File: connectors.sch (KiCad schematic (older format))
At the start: 43 parts, among them J10 70543-0001, J11 70543-0001, J12 70543-0001, J13 70543-0001, J14 70543-0003, J15 Conn_02x20_Odd_Even, J22 70543-0002, J23 70543-0002, J24 70543-0002, J5 20021121-00010C4LF, J6 70543-0001, J7 70543-0001, J8 70543-0001, J9 70543-0001

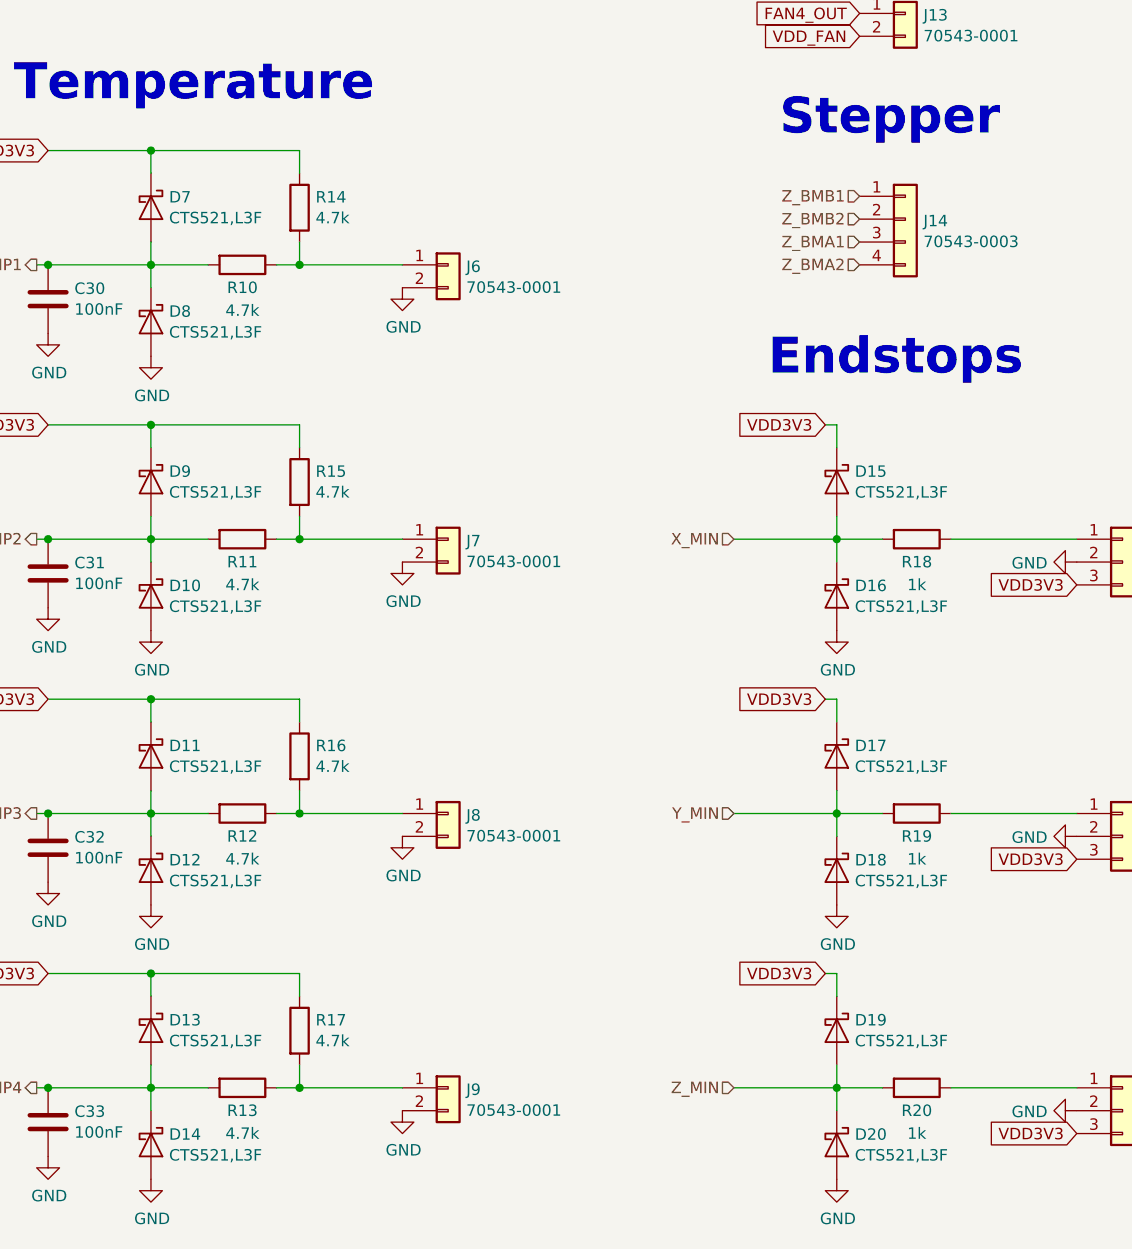
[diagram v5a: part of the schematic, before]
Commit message: Various changes
* Add Status LED
* Switched small diodes to more general available BAT54 in SOD123
* Fixed various DRC errors
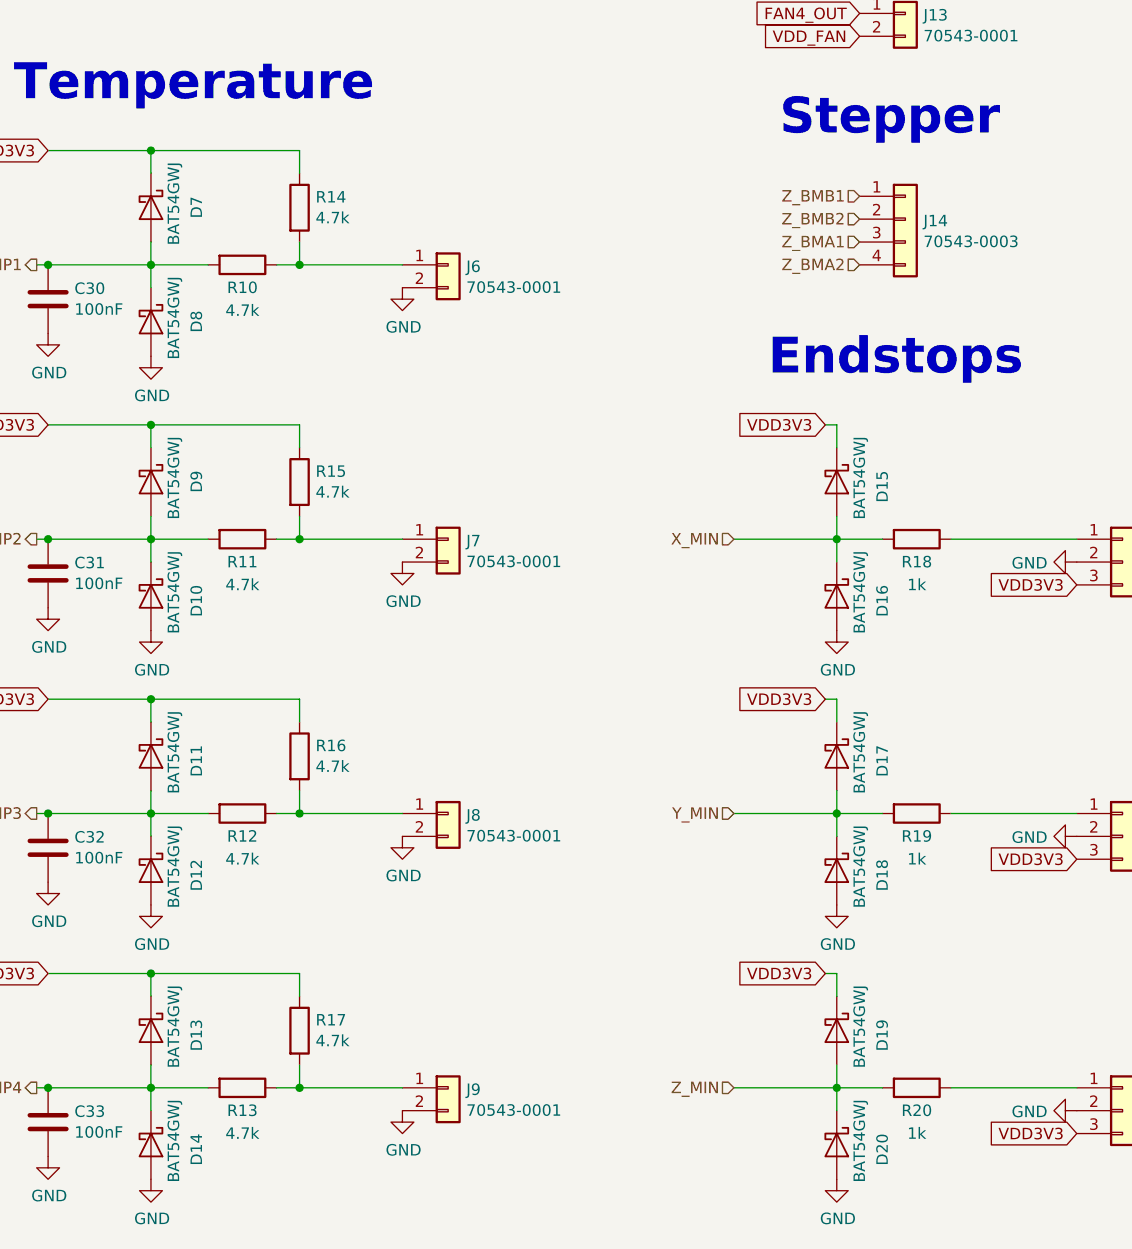
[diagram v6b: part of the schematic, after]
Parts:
- D10, D11, D12, D13, D14, D15, D16, D17, D18, D19, D20, D7, D8, D9: value CTS521,L3F -> BAT54GWJ; footprint heteromycin:SOD882 -> Diode_SMD:D_SOD-123

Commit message: Complete functional design
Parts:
- renumbered C30 to C110, C31 to C111, C32 to C112, C33 to C113, D7 to D19, D8 to D20, D9 to D21, D10 to D22, D11 to D23, D12 to D24, D13 to D25, D14 to D26, D15 to D27, D16 to D28, D17 to D29, D18 to D30, D19 to D31, D20 to D32, J5 to J11, J6 to J12, J7 to J13, J8 to J14, J9 to J15, J10 to J16, J11 to J17, J12 to J18, J13 to J19, J14 to J20, J22 to J21, J23 to J22, J24 to J23, J15 to J24, R10 to R117, R11 to R118, R12 to R119, R13 to R120, R14 to R121, R15 to R122, R16 to R123, R17 to R124, R18 to R125, R19 to R126, R20 to R127

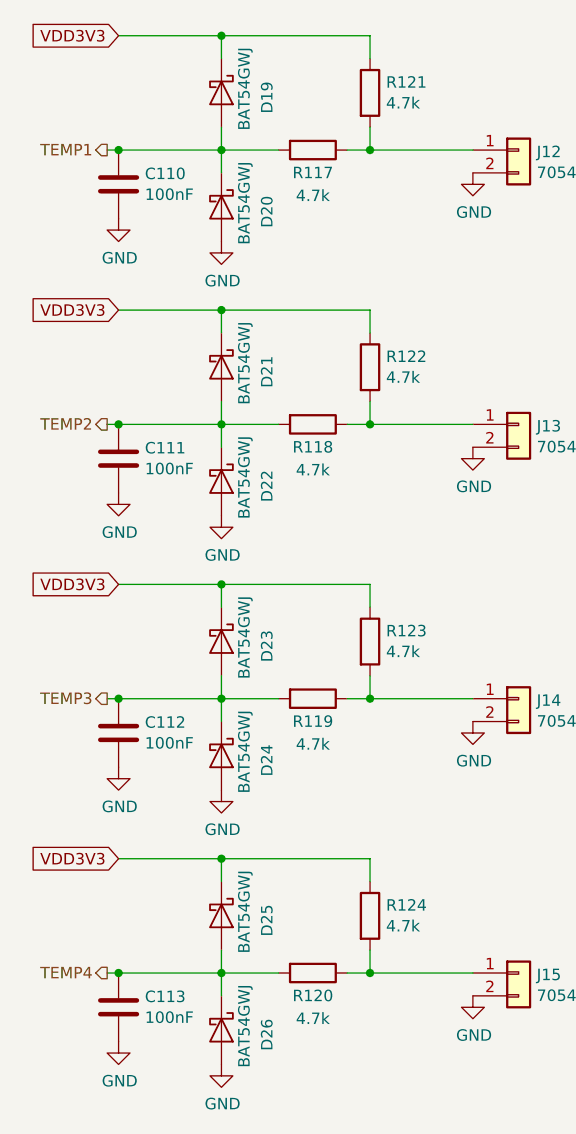
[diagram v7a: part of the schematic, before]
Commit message: Add bypass cap for I2C EEPROMs and redone some copper pour
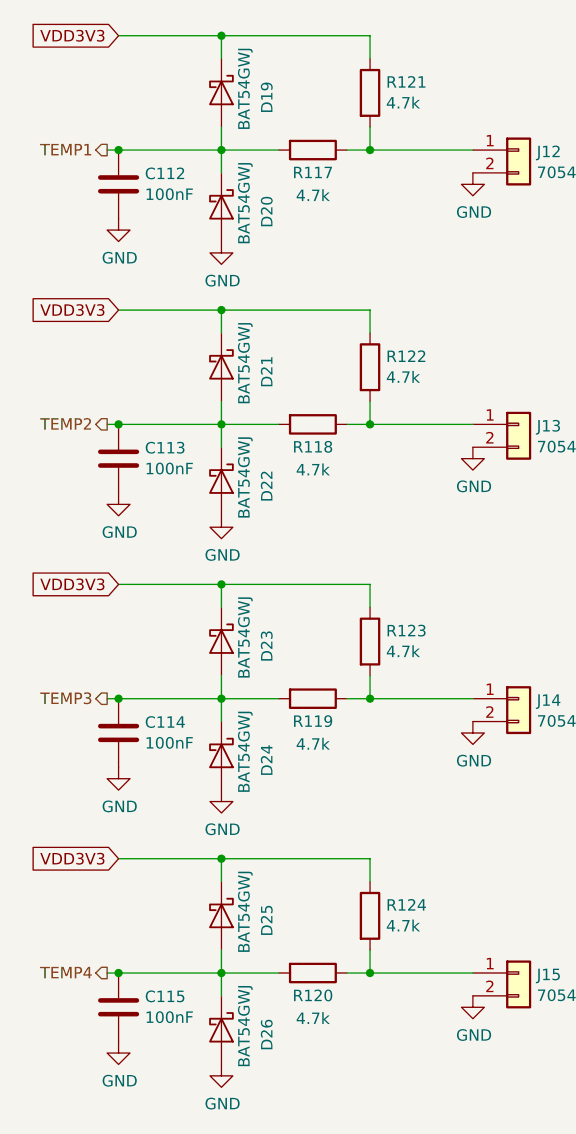
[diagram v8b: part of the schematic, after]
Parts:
- renumbered C110 to C112, C111 to C113, C112 to C114, C113 to C115
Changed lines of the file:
@@
 $EndComp
 $Comp
-L power:GND #PWR0116
+L power:GND #PWR0118
 U 1 1 5B1719B0
 P 1500 3700
-F 0 "#PWR0116" H 1500 3450 50  0001 C CNN
+F 0 "#PWR0118" H 1500 3450 50  0001 C CNN
 F 1 "GND" H 1505 3527 50  0000 C CNN
 F 2 "" H 1500 3700 50  0001 C CNN
@@
 $EndComp
 $Comp
-L power:GND #PWR0120
+L power:GND #PWR0122
 U 1 1 5B1719CA
 P 2600 3400
-F 0 "#PWR0120" H 2600 3150 50  0001 C CNN
+F 0 "#PWR0122" H 2600 3150 50  0001 C CNN
 F 1 "GND" H 2605 3227 50  0000 C CNN
 F 2 "" H 2600 3400 50  0001 C CNN
@@
 $EndComp
 $Comp
-L Device:C C110
+L Device:C C112
 U 1 1 5B1719D4
 P 1050 3450
-F 0 "C110" H 1165 3496 50  0000 L CNN
+F 0 "C112" H 1165 3496 50  0000 L CNN
 F 1 "100nF" H 1165 3405 50  0000 L CNN
 F 2 "Capacitor_SMD:C_0603_1608Metric" H 1088 3300 50  0001 C CNN
@@
 	1000 3300 1050 3300
 $Comp
-L power:GND #PWR0111
+L power:GND #PWR0113
 U 1 1 5B1719DF
 P 1050 3600
-F 0 "#PWR0111" H 1050 3350 50  0001 C CNN
+F 0 "#PWR0113" H 1050 3350 50  0001 C CNN
 F 1 "GND" H 1055 3427 50  0000 C CNN
 F 2 "" H 1050 3600 50  0001 C CNN
@@
 TEMP2
 $Comp
-L power:GND #PWR0121
+L power:GND #PWR0123
 U 1 1 5B171A2B
 P 2600 4600
-F 0 "#PWR0121" H 2600 4350 50  0001 C CNN
+F 0 "#PWR0123" H 2600 4350 50  0001 C CNN
 F 1 "GND" H 2605 4427 50  0000 C CNN
 F 2 "" H 2600 4600 50  0001 C CNN
@@
 TEMP3
 $Comp
-L power:GND #PWR0122
+L power:GND #PWR0124
 U 1 1 5B171A8C
 P 2600 5800
-F 0 "#PWR0122" H 2600 5550 50  0001 C CNN
+F 0 "#PWR0124" H 2600 5550 50  0001 C CNN
 F 1 "GND" H 2605 5627 50  0000 C CNN
 F 2 "" H 2600 5800 50  0001 C CNN
@@
 $EndComp
 $Comp
-L power:GND #PWR0115
+L power:GND #PWR0117
 U 1 1 5B17C4C4
 P 1150 1850
-F 0 "#PWR0115" H 1150 1600 50  0001 C CNN
+F 0 "#PWR0117" H 1150 1600 50  0001 C CNN
 F 1 "GND" H 1155 1677 50  0000 C CNN
 F 2 "" H 1150 1850 50  0001 C CNN
@@
 $EndComp
 $Comp
-L power:GND #PWR0124
+L power:GND #PWR0126
 U 1 1 5B40FD91
 P 4500 4900
-F 0 "#PWR0124" H 4500 4650 50  0001 C CNN
+F 0 "#PWR0126" H 4500 4650 50  0001 C CNN
 F 1 "GND" H 4505 4727 50  0000 C CNN
 F 2 "" H 4500 4900 50  0001 C CNN
@@
 $EndComp
 $Comp
-L power:GND #PWR0125
+L power:GND #PWR0127
 U 1 1 5B453620
 P 4500 6100
-F 0 "#PWR0125" H 4500 5850 50  0001 C CNN
+F 0 "#PWR0127" H 4500 5850 50  0001 C CNN
 F 1 "GND" H 4505 5927 50  0000 C CNN
 F 2 "" H 4500 6100 50  0001 C CNN
@@
 $EndComp
 $Comp
-L power:GND #PWR0126
+L power:GND #PWR0128
 U 1 1 5B457725
 P 4500 7300
-F 0 "#PWR0126" H 4500 7050 50  0001 C CNN
+F 0 "#PWR0128" H 4500 7050 50  0001 C CNN
 F 1 "GND" H 4505 7127 50  0000 C CNN
 F 2 "" H 4500 7300 50  0001 C CNN
@@
 $EndComp
 $Comp
-L power:GND #PWR0117
+L power:GND #PWR0119
 U 1 1 5B565802
 P 1500 4900
-F 0 "#PWR0117" H 1500 4650 50  0001 C CNN
+F 0 "#PWR0119" H 1500 4650 50  0001 C CNN
 F 1 "GND" H 1505 4727 50  0000 C CNN
 F 2 "" H 1500 4900 50  0001 C CNN
@@
 	2150 4500 2150 4400
 $Comp
-L Device:C C111
+L Device:C C113
 U 1 1 5B56580A
 P 1050 4650
-F 0 "C111" H 1165 4696 50  0000 L CNN
+F 0 "C113" H 1165 4696 50  0000 L CNN
 F 1 "100nF" H 1165 4605 50  0000 L CNN
 F 2 "Capacitor_SMD:C_0603_1608Metric" H 1088 4500 50  0001 C CNN
@@
 	1000 4500 1050 4500
 $Comp
-L power:GND #PWR0112
+L power:GND #PWR0114
 U 1 1 5B565812
 P 1050 4800
-F 0 "#PWR0112" H 1050 4550 50  0001 C CNN
+F 0 "#PWR0114" H 1050 4550 50  0001 C CNN
 F 1 "GND" H 1055 4627 50  0000 C CNN
 F 2 "" H 1050 4800 50  0001 C CNN
@@
 $EndComp
 $Comp
-L power:GND #PWR0118
+L power:GND #PWR0120
 U 1 1 5B57C5C8
 P 1500 6100
-F 0 "#PWR0118" H 1500 5850 50  0001 C CNN
+F 0 "#PWR0120" H 1500 5850 50  0001 C CNN
 F 1 "GND" H 1505 5927 50  0000 C CNN
 F 2 "" H 1500 6100 50  0001 C CNN
@@
 	2150 5700 2150 5600
 $Comp
-L Device:C C112
+L Device:C C114
 U 1 1 5B57C5D0
 P 1050 5850
-F 0 "C112" H 1165 5896 50  0000 L CNN
+F 0 "C114" H 1165 5896 50  0000 L CNN
 F 1 "100nF" H 1165 5805 50  0000 L CNN
 F 2 "Capacitor_SMD:C_0603_1608Metric" H 1088 5700 50  0001 C CNN
@@
 	1000 5700 1050 5700
 $Comp
-L power:GND #PWR0113
+L power:GND #PWR0115
 U 1 1 5B57C5D8
 P 1050 6000
-F 0 "#PWR0113" H 1050 5750 50  0001 C CNN
+F 0 "#PWR0115" H 1050 5750 50  0001 C CNN
 F 1 "GND" H 1055 5827 50  0000 C CNN
 F 2 "" H 1050 6000 50  0001 C CNN
@@
 TEMP4
 $Comp
-L power:GND #PWR0123
+L power:GND #PWR0125
 U 1 1 5BC9839A
 P 2600 7000
-F 0 "#PWR0123" H 2600 6750 50  0001 C CNN
+F 0 "#PWR0125" H 2600 6750 50  0001 C CNN
 F 1 "GND" H 2605 6827 50  0000 C CNN
 F 2 "" H 2600 7000 50  0001 C CNN
@@
 $EndComp
 $Comp
-L power:GND #PWR0119
+L power:GND #PWR0121
 U 1 1 5BC983B5
 P 1500 7300
-F 0 "#PWR0119" H 1500 7050 50  0001 C CNN
+F 0 "#PWR0121" H 1500 7050 50  0001 C CNN
 F 1 "GND" H 1505 7127 50  0000 C CNN
 F 2 "" H 1500 7300 50  0001 C CNN
@@
 	2150 6900 2150 6800
 $Comp
-L Device:C C113
+L Device:C C115
 U 1 1 5BC983BD
 P 1050 7050
-F 0 "C113" H 1165 7096 50  0000 L CNN
+F 0 "C115" H 1165 7096 50  0000 L CNN
 F 1 "100nF" H 1165 7005 50  0000 L CNN
 F 2 "Capacitor_SMD:C_0603_1608Metric" H 1088 6900 50  0001 C CNN
@@
 	1000 6900 1050 6900
 $Comp
-L power:GND #PWR0114
+L power:GND #PWR0116
 U 1 1 5BC983C5
 P 1050 7200
-F 0 "#PWR0114" H 1050 6950 50  0001 C CNN
+F 0 "#PWR0116" H 1050 6950 50  0001 C CNN
 F 1 "GND" H 1055 7027 50  0000 C CNN
 F 2 "" H 1050 7200 50  0001 C CNN
@@
 VDD3V3
 $Comp
-L power:GND #PWR0129
+L power:GND #PWR0131
 U 1 1 5BCB635E
 P 5550 7000
-F 0 "#PWR0129" H 5550 6750 50  0001 C CNN
+F 0 "#PWR0131" H 5550 6750 50  0001 C CNN
 F 1 "GND" V 5555 6872 50  0000 R CNN
 F 2 "" H 5550 7000 50  0001 C CNN
@@
 $EndComp
 $Comp
-L power:GND #PWR0128
+L power:GND #PWR0130
 U 1 1 5BCB65D2
 P 5550 5800
-F 0 "#PWR0128" H 5550 5550 50  0001 C CNN
+F 0 "#PWR0130" H 5550 5550 50  0001 C CNN
 F 1 "GND" V 5555 5672 50  0000 R CNN
 F 2 "" H 5550 5800 50  0001 C CNN
@@
 VDD3V3
 $Comp
-L power:GND #PWR0127
+L power:GND #PWR0129
 U 1 1 5BCBB169
 P 5550 4600
-F 0 "#PWR0127" H 5550 4350 50  0001 C CNN
+F 0 "#PWR0129" H 5550 4350 50  0001 C CNN
 F 1 "GND" V 5555 4472 50  0000 R CNN
 F 2 "" H 5550 4600 50  0001 C CNN
@@
 VDD5V
 $Comp
-L power:GND #PWR0130
+L power:GND #PWR0132
 U 1 1 5BCCC745
 P 7500 3250
-F 0 "#PWR0130" H 7500 3000 50  0001 C CNN
+F 0 "#PWR0132" H 7500 3000 50  0001 C CNN
 F 1 "GND" H 7505 3077 50  0000 C CNN
 F 2 "" H 7500 3250 50  0001 C CNN
@@
 $EndComp
 $Comp
-L power:GND #PWR0131
+L power:GND #PWR0133
 U 1 1 5BCCC827
 P 9250 3250
-F 0 "#PWR0131" H 9250 3000 50  0001 C CNN
+F 0 "#PWR0133" H 9250 3000 50  0001 C CNN
 F 1 "GND" H 9255 3077 50  0000 C CNN
 F 2 "" H 9250 3250 50  0001 C CNN
